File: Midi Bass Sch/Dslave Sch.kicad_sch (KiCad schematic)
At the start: 11 parts

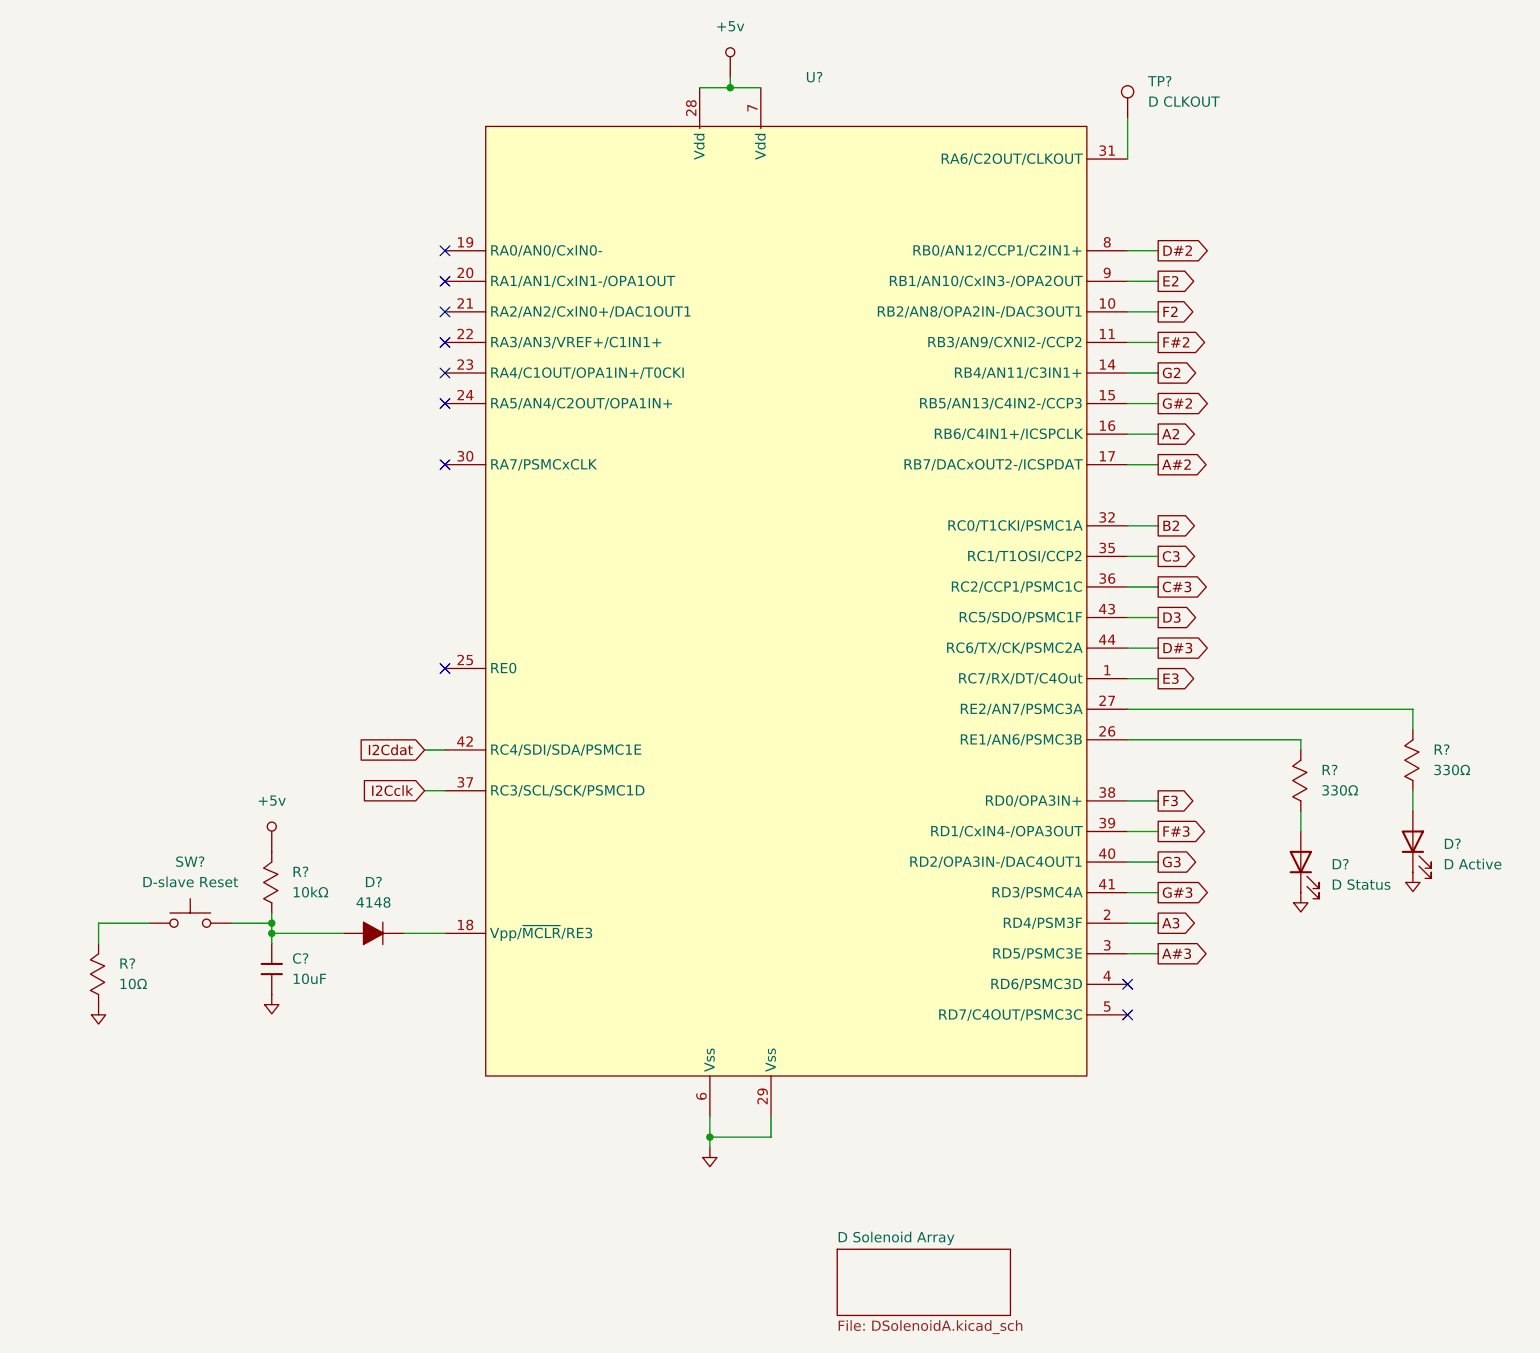
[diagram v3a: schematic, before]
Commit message: added solenoid array for the G slave
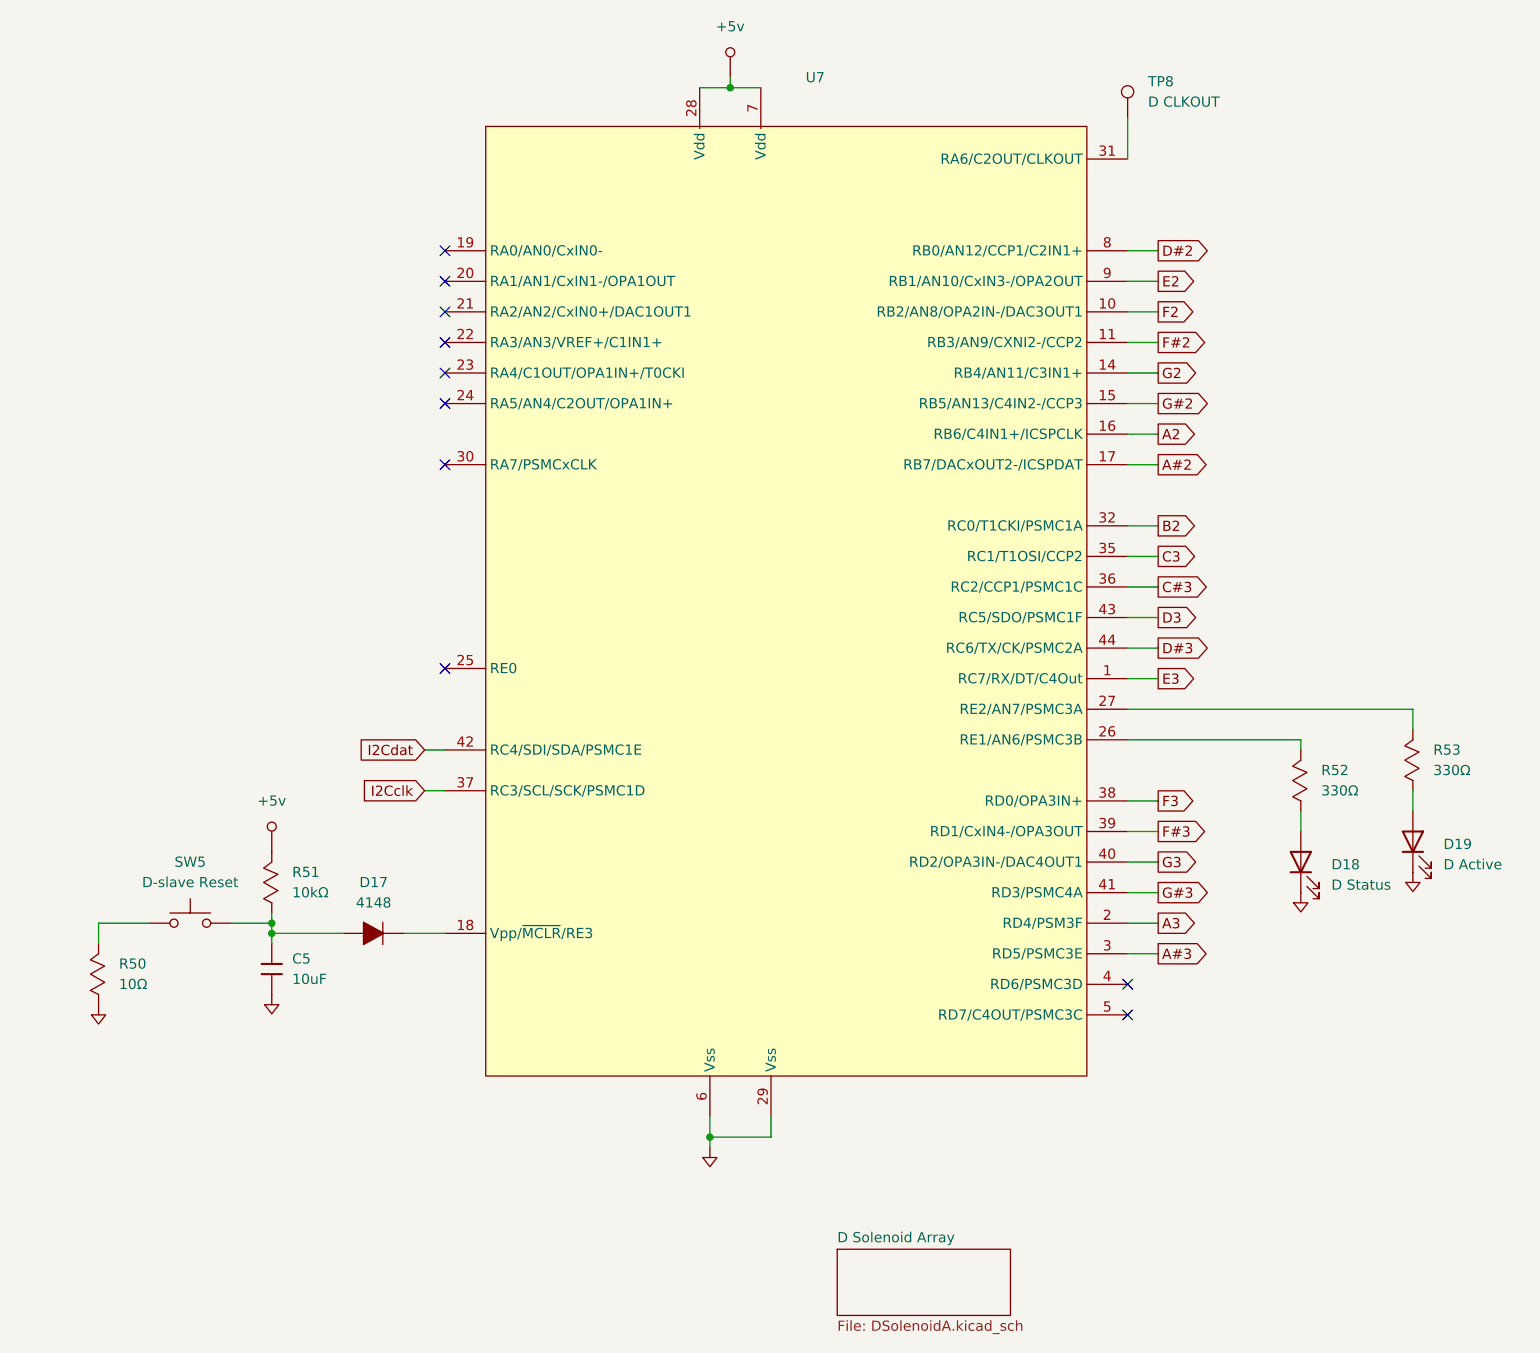
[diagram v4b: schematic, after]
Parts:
- gave numbers to parts that had none: 11
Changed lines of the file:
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@@
 		(dnp no)
 		(fields_autoplaced yes)
-		(property "Reference" "TP?"
+		(property "Reference" "TP8"
 			(at 157.48 27.1779 0)
 			(effects
@@
 			(project "Midi Bass Sch"
 				(path "/06818073-fb22-48ee-acc5-6dedd827034e/4e89443f-252f-4d60-96aa-3cd5b0237902"
-					(reference "TP?")
+					(reference "TP8")
 					(unit 1)
 				)
@@
 		(dnp no)
 		(fields_autoplaced yes)
-		(property "Reference" "R?"
+		(property "Reference" "R51"
 			(at 50.8 125.7299 90)
 			(effects
@@
 			(project "Midi Bass Sch"
 				(path "/06818073-fb22-48ee-acc5-6dedd827034e/4e89443f-252f-4d60-96aa-3cd5b0237902"
-					(reference "R?")
+					(reference "R51")
 					(unit 1)
 				)
@@
 		(on_board yes)
 		(dnp no)
-		(property "Reference" "U?"
+		(property "Reference" "U7"
 			(at 114.808 26.67 0)
 			(effects
@@
 			(project "Midi Bass Sch"
 				(path "/06818073-fb22-48ee-acc5-6dedd827034e/4e89443f-252f-4d60-96aa-3cd5b0237902"
-					(reference "U?")
+					(reference "U7")
 					(unit 1)
 				)
@@
 		(dnp no)
 		(fields_autoplaced yes)
-		(property "Reference" "#PWR0196"
+		(property "Reference" "#PWR072"
 			(at 190.5 124.46 0)
 			(effects
@@
 			(project "Midi Bass Sch"
 				(path "/06818073-fb22-48ee-acc5-6dedd827034e/4e89443f-252f-4d60-96aa-3cd5b0237902"
-					(reference "#PWR0196")
+					(reference "#PWR072")
 					(unit 1)
 				)
@@
 		(dnp no)
 		(fields_autoplaced yes)
-		(property "Reference" "#PWR0194"
+		(property "Reference" "#PWR070"
 			(at 110.1344 21.6916 0)
 			(effects
@@
 			(project "Midi Bass Sch"
 				(path "/06818073-fb22-48ee-acc5-6dedd827034e/4e89443f-252f-4d60-96aa-3cd5b0237902"
-					(reference "#PWR0194")
+					(reference "#PWR070")
 					(unit 1)
 				)
@@
 		(dnp no)
 		(fields_autoplaced yes)
-		(property "Reference" "R?"
+		(property "Reference" "R52"
 			(at 179.07 113.0299 90)
 			(effects
@@
 			(project "Midi Bass Sch"
 				(path "/06818073-fb22-48ee-acc5-6dedd827034e/4e89443f-252f-4d60-96aa-3cd5b0237902"
-					(reference "R?")
+					(reference "R52")
 					(unit 1)
 				)
@@
 		(dnp no)
 		(fields_autoplaced yes)
-		(property "Reference" "SW?"
+		(property "Reference" "SW5"
 			(at 38.1 124.46 0)
 			(effects
@@
 			(project "Midi Bass Sch"
 				(path "/06818073-fb22-48ee-acc5-6dedd827034e/4e89443f-252f-4d60-96aa-3cd5b0237902"
-					(reference "SW?")
+					(reference "SW5")
 					(unit 1)
 				)
@@
 		(dnp no)
 		(fields_autoplaced yes)
-		(property "Reference" "R?"
+		(property "Reference" "R53"
 			(at 193.04 110.4899 90)
 			(effects
@@
 			(project "Midi Bass Sch"
 				(path "/06818073-fb22-48ee-acc5-6dedd827034e/4e89443f-252f-4d60-96aa-3cd5b0237902"
-					(reference "R?")
+					(reference "R53")
 					(unit 1)
 				)
@@
 		(dnp no)
 		(fields_autoplaced yes)
-		(property "Reference" "R?"
+		(property "Reference" "R50"
 			(at 29.21 137.1599 90)
 			(effects
@@
 			(project "Midi Bass Sch"
 				(path "/06818073-fb22-48ee-acc5-6dedd827034e/4e89443f-252f-4d60-96aa-3cd5b0237902"
-					(reference "R?")
+					(reference "R50")
 					(unit 1)
 				)
@@
 		(dnp no)
 		(fields_autoplaced yes)
-		(property "Reference" "D?"
+		(property "Reference" "D18"
 			(at 180.34 124.7774 90)
 			(effects
@@
 			(project "Midi Bass Sch"
 				(path "/06818073-fb22-48ee-acc5-6dedd827034e/4e89443f-252f-4d60-96aa-3cd5b0237902"
-					(reference "D?")
+					(reference "D18")
 					(unit 1)
 				)
@@
 		(dnp no)
 		(fields_autoplaced yes)
-		(property "Reference" "D?"
+		(property "Reference" "D19"
 			(at 194.31 122.2374 90)
 			(effects
@@
 			(project "Midi Bass Sch"
 				(path "/06818073-fb22-48ee-acc5-6dedd827034e/4e89443f-252f-4d60-96aa-3cd5b0237902"
-					(reference "D?")
+					(reference "D19")
 					(unit 1)
 				)
@@
 		(dnp no)
 		(fields_autoplaced yes)
-		(property "Reference" "C?"
+		(property "Reference" "C5"
 			(at 50.8 136.5249 0)
 			(effects
@@
 			(project "Midi Bass Sch"
 				(path "/06818073-fb22-48ee-acc5-6dedd827034e/4e89443f-252f-4d60-96aa-3cd5b0237902"
-					(reference "C?")
+					(reference "C5")
 					(unit 1)
 				)
@@
 		(dnp no)
 		(fields_autoplaced yes)
-		(property "Reference" "D?"
+		(property "Reference" "D17"
 			(at 60.96 127 90)
 			(effects
@@
 			(project "Midi Bass Sch"
 				(path "/06818073-fb22-48ee-acc5-6dedd827034e/4e89443f-252f-4d60-96aa-3cd5b0237902"
-					(reference "D?")
+					(reference "D17")
 					(unit 1)
 				)
@@
 		(dnp no)
 		(fields_autoplaced yes)
-		(property "Reference" "#PWR0195"
+		(property "Reference" "#PWR071"
 			(at 176.53 127 0)
 			(effects
@@
 			(project "Midi Bass Sch"
 				(path "/06818073-fb22-48ee-acc5-6dedd827034e/4e89443f-252f-4d60-96aa-3cd5b0237902"
-					(reference "#PWR0195")
-					(unit 1)
-				)
+					(reference "#PWR071")
+					(unit 1)
+				)

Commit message: added program pins to all processors
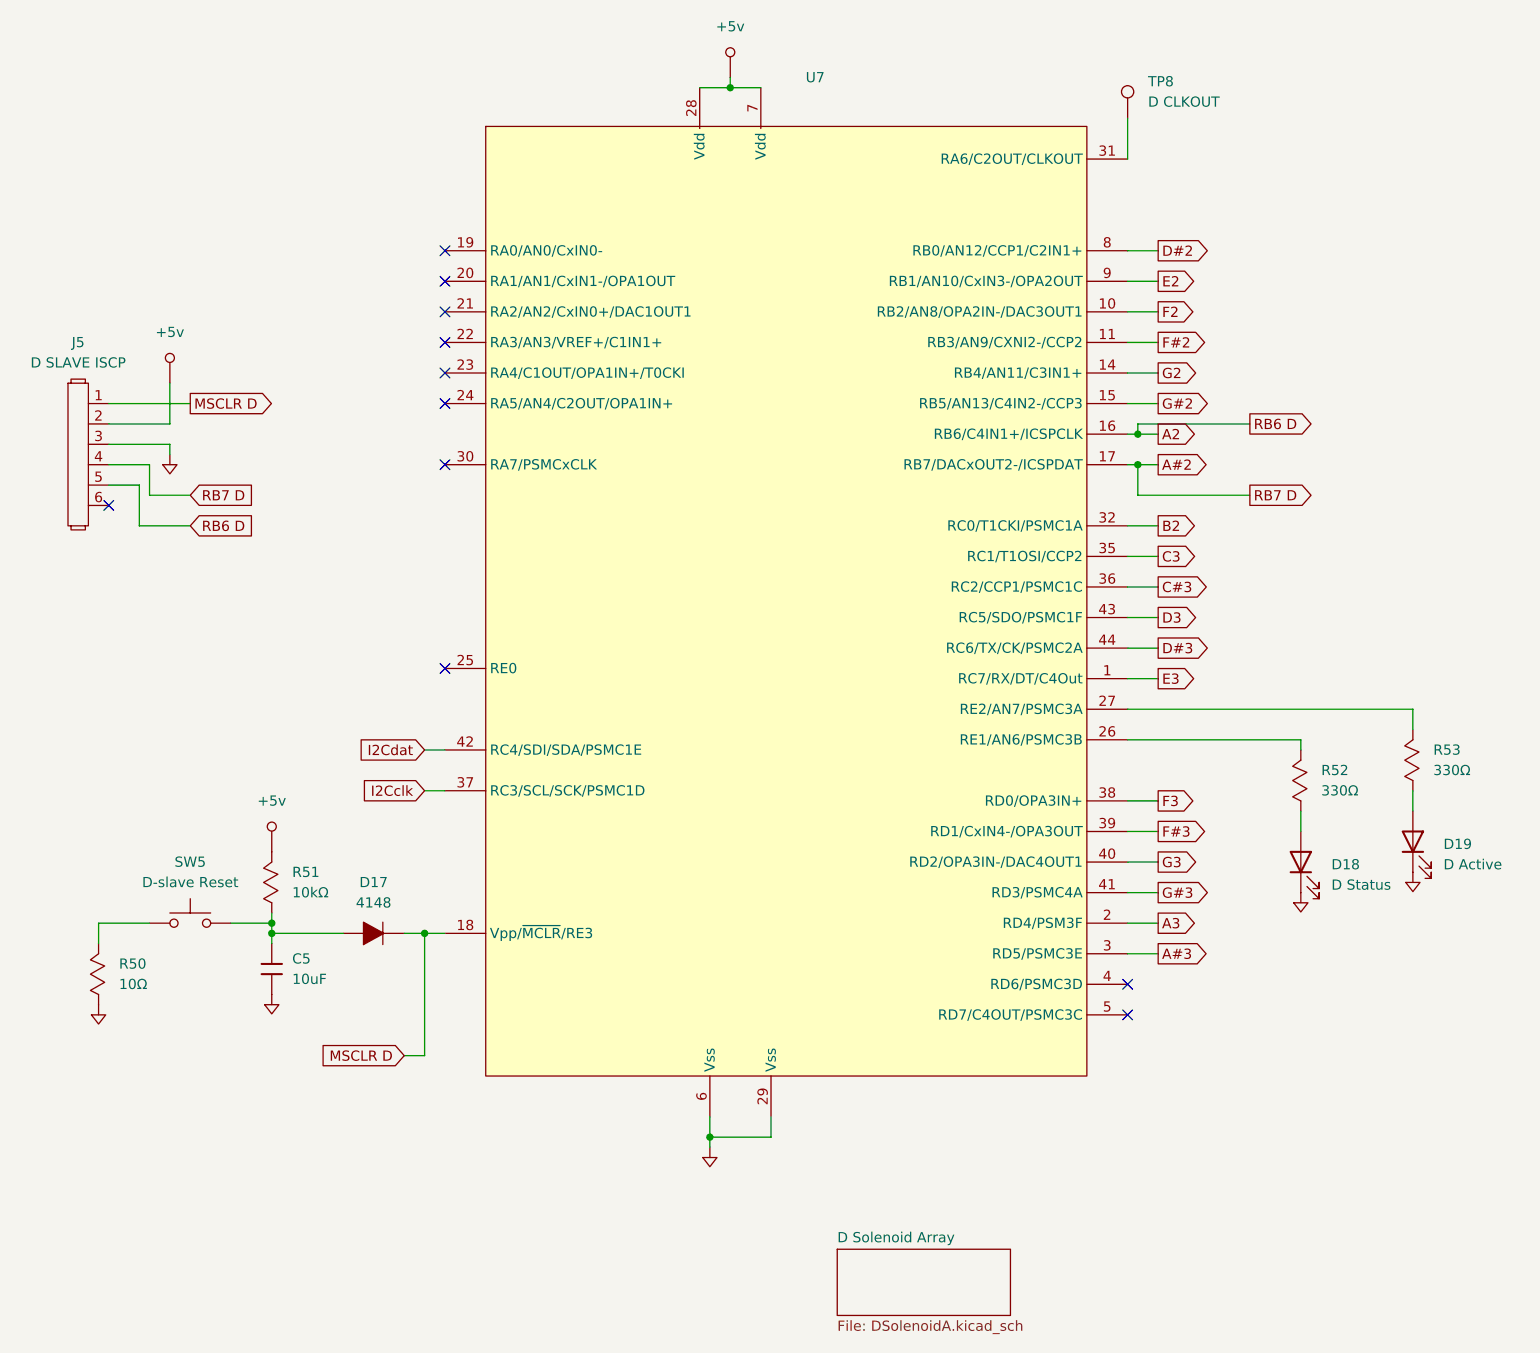
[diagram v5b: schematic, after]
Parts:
- added J5: D SLAVE ISCP, symbol Owen's Symbols:Header_1x6
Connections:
- net +5v: now also J5.2
- net A#2: now also J5.4
- net A2: now also J5.5
- net GND: now also J5.3
- net MSCLR D: now reaches D17.2, U7.18 (Vpp/~{MCLR}/RE3)
- net MSCLR D: now also J5.1
- no-connect marks 10 -> 11

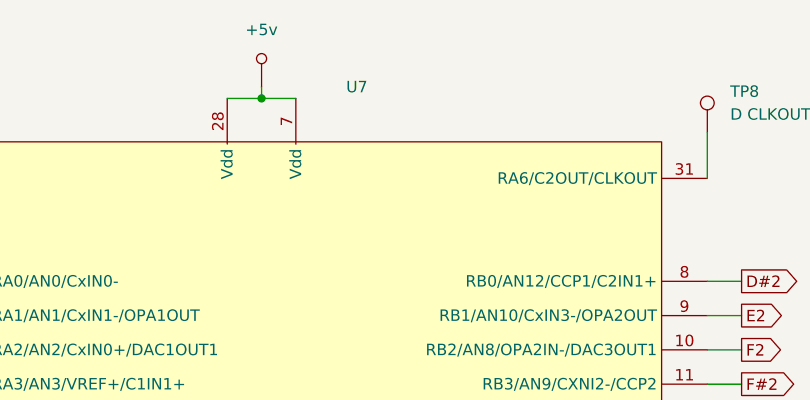
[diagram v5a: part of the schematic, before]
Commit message: added footprints to kicad schematic still need footprint for din connector
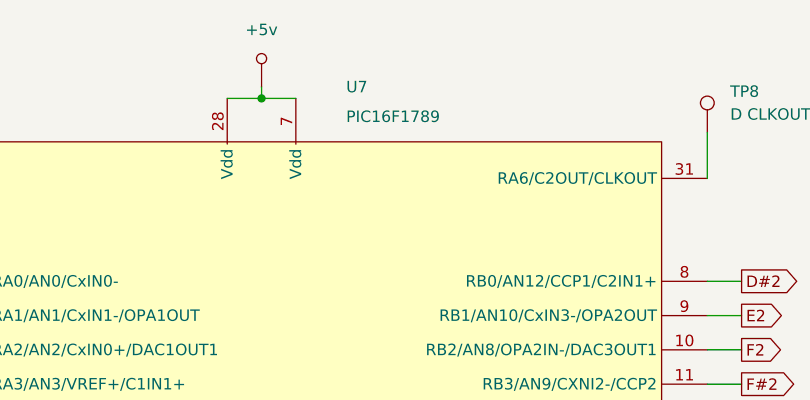
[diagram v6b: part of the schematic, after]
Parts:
- C5: footprint (none) -> Capacitor_SMD:C_0805_2012Metric_Pad1.18x1.45mm_HandSolder
- D17, D18, D19: footprint (none) -> Diode_SMD:D_0805_2012Metric_Pad1.15x1.40mm_HandSolder
- J5: footprint (none) -> Connector_PinHeader_2.54mm:PinHeader_1x06_P2.54mm_Vertical
- R50, R51, R52, R53: footprint (none) -> Resistor_SMD:R_0805_2012Metric_Pad1.20x1.40mm_HandSolder
- U7: value ~ -> PIC16F1789
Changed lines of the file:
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@@
 			)
 		)
-		(property "Footprint" ""
+		(property "Footprint" "Resistor_SMD:R_0805_2012Metric_Pad1.20x1.40mm_HandSolder"
 			(at 45.72 128.27 0)
 			(effects
@@
 			)
 		)
-		(property "Value" "~"
-			(at 120.3041 154.94 0)
+		(property "Value" "PIC16F1789"
+			(at 114.808 29.972 0)
 			(effects
 				(font
@@
 			)
 		)
-		(property "Footprint" ""
+		(property "Footprint" "Resistor_SMD:R_0805_2012Metric_Pad1.20x1.40mm_HandSolder"
 			(at 173.99 115.57 0)
 			(effects
@@
 			)
 		)
-		(property "Footprint" ""
+		(property "Footprint" "Resistor_SMD:R_0805_2012Metric_Pad1.20x1.40mm_HandSolder"
 			(at 187.96 113.03 0)
 			(effects
@@
 			)
 		)
-		(property "Footprint" ""
+		(property "Footprint" "Resistor_SMD:R_0805_2012Metric_Pad1.20x1.40mm_HandSolder"
 			(at 24.13 139.7 0)
 			(effects
@@
 			)
 		)
-		(property "Footprint" ""
+		(property "Footprint" "Diode_SMD:D_0805_2012Metric_Pad1.15x1.40mm_HandSolder"
 			(at 176.53 124.46 0)
 			(effects
@@
 			)
 		)
-		(property "Footprint" ""
+		(property "Footprint" "Diode_SMD:D_0805_2012Metric_Pad1.15x1.40mm_HandSolder"
 			(at 190.5 121.92 0)
 			(effects
@@
 			)
 		)
-		(property "Footprint" ""
+		(property "Footprint" "Capacitor_SMD:C_0805_2012Metric_Pad1.18x1.45mm_HandSolder"
 			(at 48.26 132.08 0)
 			(effects
@@
 			)
 		)
-		(property "Footprint" ""
+		(property "Footprint" "Diode_SMD:D_0805_2012Metric_Pad1.15x1.40mm_HandSolder"
 			(at 57.15 133.35 0)
 			(effects
@@
 			)
 		)
-		(property "Footprint" ""
+		(property "Footprint" "Connector_PinHeader_2.54mm:PinHeader_1x06_P2.54mm_Vertical"
 			(at 24.13 63.5 0)
 			(effects
